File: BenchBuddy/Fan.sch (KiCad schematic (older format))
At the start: 0 parts

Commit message: Week3 part 1
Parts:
- added Q?: MOSFET_N, ~, symbol MOSFET_N
- added R? (x5): R, ~, symbol R
- added RV?: POT, ~, symbol POT
- added U?: LM324, symbol LM324
- added U?: MCP4922-E/P, DIP14, symbol MCP4922-E/P
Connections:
- net labels added: +12V, -12V, AGND, CS_N, Current Measure, MISO, MOSI, SLCK
- wire segments 0 -> 34

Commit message: Week3 Part 2
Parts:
- removed R? (x3): R, ~, symbol R
- removed RV?: POT, ~, symbol POT
- added D?: DIODE, ~, symbol DIODE
- added Q? (x2): MOSFET_N, ~, symbol MOSFET_N
- added TH?: THERMISTOR, ~, symbol THERMISTOR
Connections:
- net labels added: +12C, CURR_MEAS, FAN_MODE, FAN_PWM, Fan_Out+, Fan_Out-, Tach_In, Tach_MEASURE
- net labels removed: Current Measure, Fan_IN, Power+, Power-, Tach, Tach_OUT
- wire segments 34 -> 36
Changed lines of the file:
@@
 EESchema Schematic File Version 2
+LIBS:BenchBuddy
 LIBS:power
 LIBS:device
@@
 $Descr A4 11693 8268
 encoding utf-8
-Sheet 7 9
+Sheet 9 9
 Title ""
-Date "5 mar 2014"
+Date "7 mar 2014"
 Rev ""
 Comp ""
@@
 Comment4 ""
 $EndDescr
-Text HLabel 9800 3350 0    60   Output ~ 0
-Power+
-Text HLabel 9800 3650 0    60   Input ~ 0
-Power-
-Text HLabel 9750 3900 0    60   Input ~ 0
-Tach
-Text HLabel 1300 4300 0    60   Output ~ 0
-Tach_OUT
+Text HLabel 9800 2000 2    60   Output ~ 0
+Fan_Out+
+Text HLabel 9800 2150 2    60   Output ~ 0
+Fan_Out-
+Text HLabel 9800 6150 2    60   Input ~ 0
+Tach_In
+Text HLabel 1250 6150 0    60   Output ~ 0
+Tach_MEASURE
 Text HLabel 1300 4050 0    60   Input ~ 0
-Fan_IN
+FAN_PWM
 $Comp
 L LM324 U?
@@
 F 3 "~" H 7550 2550 60  0000 C CNN
 	1    7550 2550
-	1    0    0    -1
-$EndComp
-$Comp
-L +12V #PWR?
-U 1 1 531512F4
-P 7650 1950
-F 0 "#PWR?" H 7650 1900 20  0001 C CNN
-F 1 "+12V" H 7650 2050 30  0000 C CNN
-F 2 "" H 7650 1950 60  0000 C CNN
-F 3 "" H 7650 1950 60  0000 C CNN
-	1    7650 1950
 	1    0    0    -1
 $EndComp
@@
 $EndComp
 $Comp
-L R R?
-U 1 1 53151457
-P 4650 2150
-F 0 "R?" V 4730 2150 40  0000 C CNN
-F 1 "R" V 4657 2151 40  0000 C CNN
-F 2 "~" V 4580 2150 30  0000 C CNN
-F 3 "~" H 4650 2150 30  0000 C CNN
-	1    4650 2150
-	1    0    0    -1
-$EndComp
-$Comp
 L +12V #PWR?
 U 1 1 53151465
@@
 	6700 2550 7350 2550
 Wire Wire Line
-	7650 1950 7650 2350
-Wire Wire Line
-	7650 2750 7650 3350
-Wire Wire Line
-	7650 3350 9800 3350
-Wire Wire Line
-	5550 3650 9800 3650
-Wire Wire Line
-	7650 3650 7650 4100
-Wire Wire Line
 	7650 4600 7650 4900
 Wire Wire Line
-	5550 3650 5550 2650
-Wire Wire Line
 	5550 2650 5700 2650
-Connection ~ 7650 3650
 Wire Wire Line
 	6100 3150 6100 2950
@@
 Wire Wire Line
 	4400 2450 5700 2450
-Wire Wire Line
-	4650 2400 4650 3000
-Connection ~ 4650 2450
-$Comp
-L POT RV?
-U 1 1 531514B9
-P 4650 3250
-F 0 "RV?" H 4650 3150 50  0000 C CNN
-F 1 "POT" H 4650 3250 50  0000 C CNN
-F 2 "~" H 4650 3250 60  0000 C CNN
-F 3 "~" H 4650 3250 60  0000 C CNN
-	1    4650 3250
-	0    -1   -1   0
-$EndComp
-Wire Wire Line
-	4650 3500 4650 3850
 $Comp
 L AGND #PWR?
 U 1 1 53151500
-P 4650 3850
-F 0 "#PWR?" H 4650 3850 40  0001 C CNN
-F 1 "AGND" H 4650 3780 50  0000 C CNN
-F 2 "" H 4650 3850 60  0000 C CNN
-F 3 "" H 4650 3850 60  0000 C CNN
-	1    4650 3850
-	1    0    0    -1
-$EndComp
-Wire Wire Line
-	8200 3900 9750 3900
+P 5200 3250
+F 0 "#PWR?" H 5200 3250 40  0001 C CNN
+F 1 "AGND" H 5200 3180 50  0000 C CNN
+F 2 "" H 5200 3250 60  0000 C CNN
+F 3 "" H 5200 3250 60  0000 C CNN
+	1    5200 3250
+	1    0    0    -1
+$EndComp
 Text HLabel 1300 4150 0    60   Input ~ 0
-Current Measure
-Wire Wire Line
-	1300 4150 5650 4150
-Connection ~ 7650 4000
-$Comp
-L R R?
-U 1 1 5315166D
-P 5200 3250
-F 0 "R?" V 5280 3250 40  0000 C CNN
-F 1 "R" V 5207 3251 40  0000 C CNN
-F 2 "~" V 5130 3250 30  0000 C CNN
-F 3 "~" H 5200 3250 30  0000 C CNN
-	1    5200 3250
-	1    0    0    -1
-$EndComp
-Wire Wire Line
-	1300 4050 4950 4050
-Wire Wire Line
-	4950 4050 4950 3650
-Wire Wire Line
-	4950 3650 5200 3650
-Wire Wire Line
-	5200 3650 5200 3550
-Wire Wire Line
-	5200 3000 5200 2450
-Connection ~ 5200 2450
-Wire Wire Line
-	5650 4150 5650 4000
-Wire Wire Line
-	1300 4300 5650 4300
-Wire Wire Line
-	5650 4300 5650 5200
-Wire Wire Line
-	5650 5200 8200 5200
-Wire Wire Line
-	8200 5200 8200 3900
-Wire Wire Line
-	5650 4000 7650 4000
+CURR_MEAS
+Wire Wire Line
+	5650 4150 1300 4150
+Wire Wire Line
+	5650 3800 5650 4150
+Wire Wire Line
+	1250 6150 9800 6150
 $Comp
 L MCP4922-E/P U?
@@
 Wire Wire Line
 	2450 2600 1300 2600
-$Comp
-L R R?
-U 1 1 5315191D
-P 2450 3350
-F 0 "R?" V 2530 3350 40  0000 C CNN
-F 1 "R" V 2457 3351 40  0000 C CNN
-F 2 "~" V 2380 3350 30  0000 C CNN
-F 3 "~" H 2450 3350 30  0000 C CNN
-	1    2450 3350
-	1    0    0    -1
-$EndComp
-Wire Wire Line
-	2450 3100 2450 2800
-Wire Wire Line
-	2450 3600 2450 4050
+Wire Wire Line
+	2450 2800 2450 4050
 Connection ~ 2450 4050
+$Comp
+L MOSFET_N Q?
+U 1 1 53191BE7
+P 7050 4350
+F 0 "Q?" H 7060 4520 60  0000 R CNN
+F 1 "MOSFET_N" H 7060 4200 60  0000 R CNN
+F 2 "~" H 7050 4350 60  0000 C CNN
+F 3 "~" H 7050 4350 60  0000 C CNN
+	1    7050 4350
+	1    0    0    -1
+$EndComp
+$Comp
+L THERMISTOR TH?
+U 1 1 53191C1C
+P 7650 1350
+F 0 "TH?" V 7750 1400 50  0000 C CNN
+F 1 "THERMISTOR" V 7550 1350 50  0000 C CNN
+F 2 "~" H 7650 1350 60  0000 C CNN
+F 3 "~" H 7650 1350 60  0000 C CNN
+	1    7650 1350
+	1    0    0    -1
+$EndComp
+Wire Wire Line
+	7650 1100 7650 1000
+Wire Wire Line
+	7650 1600 7650 2000
+Wire Wire Line
+	7650 2000 9800 2000
+Wire Wire Line
+	9800 2150 7650 2150
+Wire Wire Line
+	7650 2150 7650 2350
+$Comp
+L DIODE D?
+U 1 1 53191C9A
+P 7450 2000
+F 0 "D?" H 7450 2100 40  0000 C CNN
+F 1 "DIODE" H 7450 1900 40  0000 C CNN
+F 2 "~" H 7450 2000 60  0000 C CNN
+F 3 "~" H 7450 2000 60  0000 C CNN
+	1    7450 2000
+	0    -1   -1   0
+$EndComp
+Wire Wire Line
+	7450 2200 7650 2200
+Connection ~ 7650 2200
+Wire Wire Line
+	7450 1800 7650 1800
+Connection ~ 7650 1800
+Wire Wire Line
+	7650 2750 7650 4100
+Wire Wire Line
+	7150 4150 7150 3950
+Wire Wire Line
+	7150 3950 7650 3950
+Connection ~ 7650 3950
+Wire Wire Line
+	7150 4550 7150 4750
+Wire Wire Line
+	7150 4750 7650 4750
+Connection ~ 7650 4750
+Wire Wire Line
+	5650 3800 7650 3800
+Connection ~ 7650 3800
+Wire Wire Line
+	1300 4050 3800 4050
+Wire Wire Line
+	5550 3500 7650 3500
+Connection ~ 7650 3500
+Wire Wire Line
+	5550 3500 5550 2650
+$Comp
+L MOSFET_N Q?
+U 1 1 53191E78
+P 5100 2900
+F 0 "Q?" H 5110 3070 60  0000 R CNN
+F 1 "MOSFET_N" H 5110 2750 60  0000 R CNN
+F 2 "~" H 5100 2900 60  0000 C CNN
+F 3 "~" H 5100 2900 60  0000 C CNN
+	1    5100 2900
+	1    0    0    -1
+$EndComp
+Wire Wire Line
+	5200 3250 5200 3100
+Wire Wire Line
+	5200 2700 5200 2450
+Connection ~ 5200 2450
+Wire Wire Line
+	4900 2900 3800 2900
+Wire Wire Line
+	3800 2900 3800 4050
+Text HLabel 1300 4350 0    60   Input ~ 0
+FAN_MODE
+Wire Wire Line
+	1300 4350 6850 4350
+$Comp
+L +12C #PWR?
+U 1 1 53192305
+P 7650 1000
+F 0 "#PWR?" H 7650 970 30  0001 C CNN
+F 1 "+12C" H 7650 1110 40  0000 C CNN
+F 2 "~" H 7650 1000 60  0000 C CNN
+F 3 "~" H 7650 1000 60  0000 C CNN
+	1    7650 1000
+	1    0    0    -1
+$EndComp
 $EndSCHEMATC

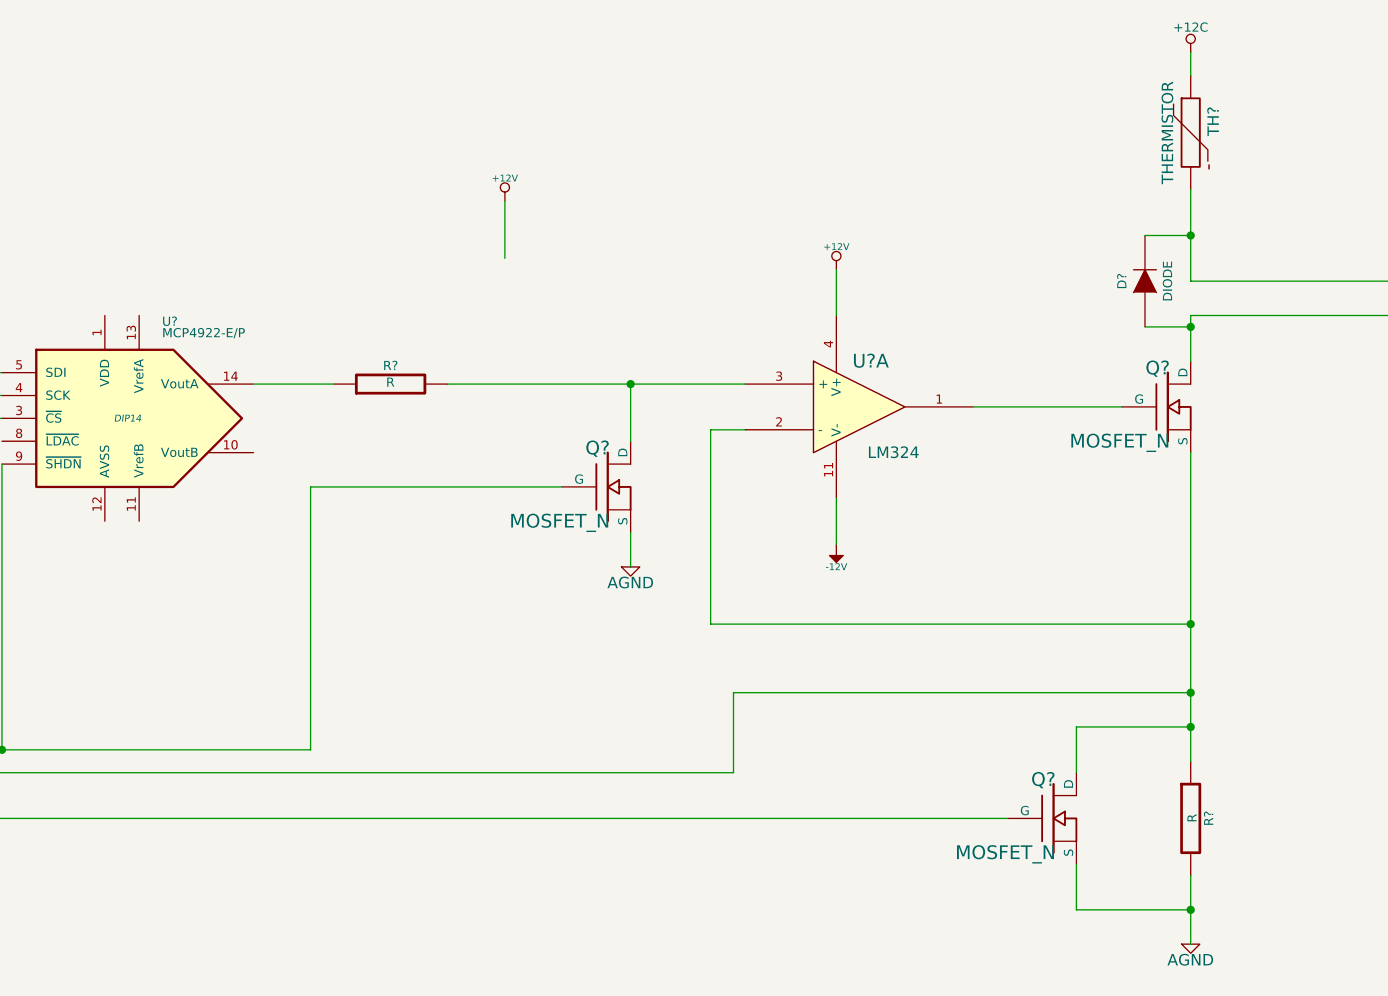
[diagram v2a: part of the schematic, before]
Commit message: Colocação dos Componentes Relé
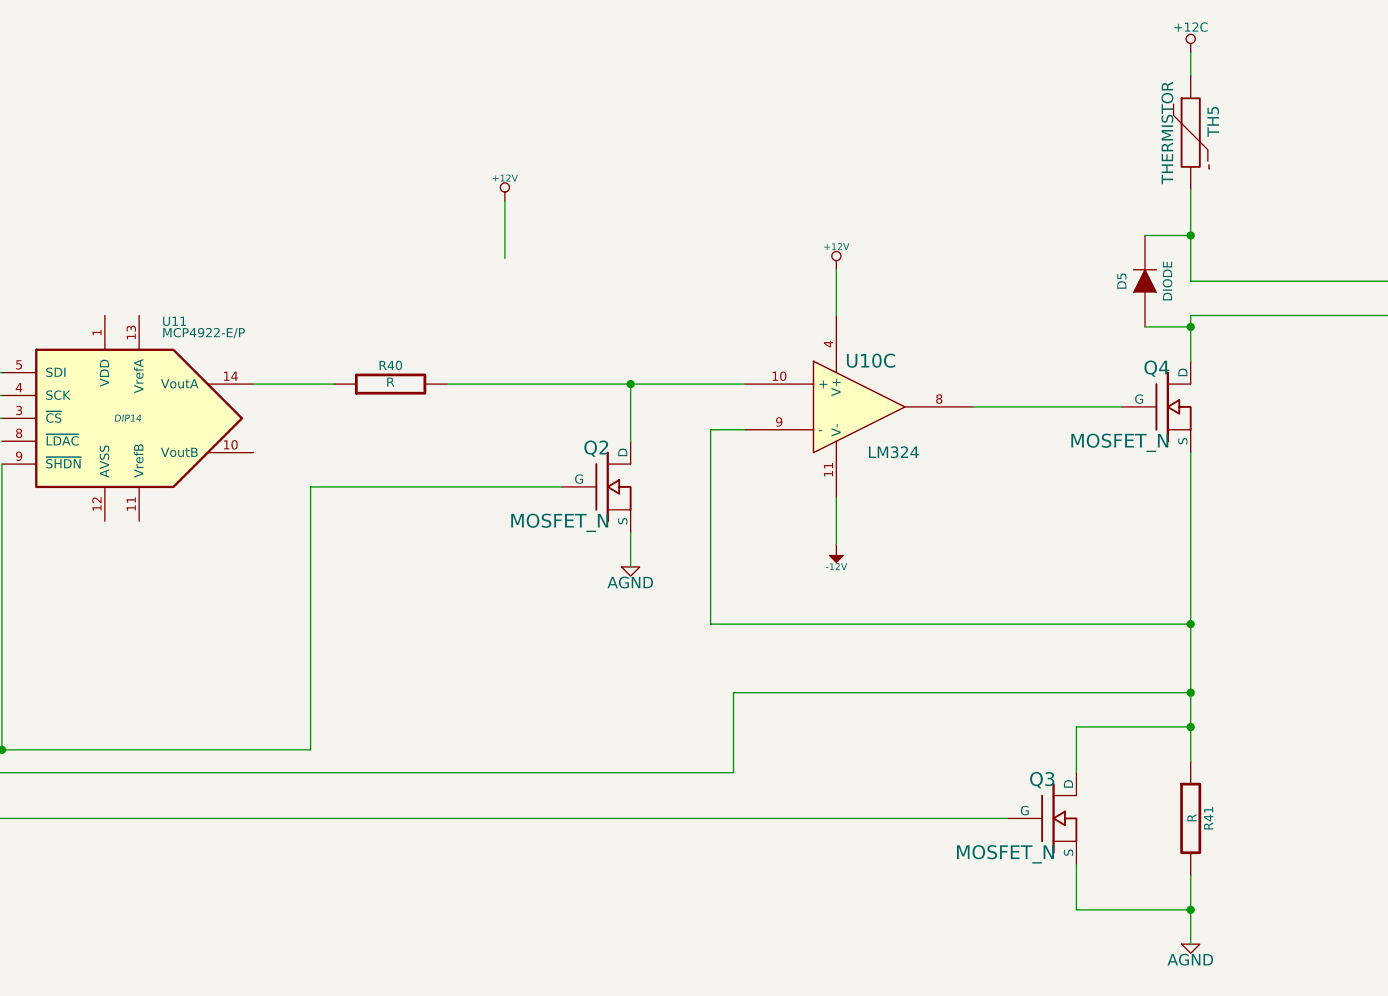
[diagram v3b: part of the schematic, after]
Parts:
- gave numbers to parts that had none: 9
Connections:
- net CURR_MEAS: now also U10.9 (-); no longer U10.2 (-)
- net at Q4.G: now also U10.8; no longer U10.1
- net at Q2.D, R40.2: now also U10.10 (+); no longer U10.3 (+)
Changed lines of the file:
@@
 Sheet 9 9
 Title ""
-Date "7 mar 2014"
+Date "9 mar 2014"
 Rev ""
 Comp ""
@@
 FAN_PWM
 $Comp
-L LM324 U?
-U 1 1 5315125A
+L LM324 U10
+U 3 1 5315125A
 P 6200 2550
-F 0 "U?" H 6250 2750 60  0000 C CNN
+F 0 "U10" H 6250 2750 60  0000 C CNN
 F 1 "LM324" H 6350 2350 50  0000 C CNN
 F 2 "" H 6200 2550 60  0000 C CNN
 F 3 "" H 6200 2550 60  0000 C CNN
-	1    6200 2550
-	1    0    0    -1
-$EndComp
-$Comp
-L MOSFET_N Q?
+	3    6200 2550
+	1    0    0    -1
+$EndComp
+$Comp
+L MOSFET_N Q4
 U 1 1 531512AB
 P 7550 2550
-F 0 "Q?" H 7560 2720 60  0000 R CNN
+F 0 "Q4" H 7560 2720 60  0000 R CNN
 F 1 "MOSFET_N" H 7560 2400 60  0000 R CNN
 F 2 "~" H 7550 2550 60  0000 C CNN
@@
 $EndComp
 $Comp
-L R R?
+L R R41
 U 1 1 53151349
 P 7650 4350
-F 0 "R?" V 7730 4350 40  0000 C CNN
+F 0 "R41" V 7730 4350 40  0000 C CNN
 F 1 "R" V 7657 4351 40  0000 C CNN
 F 2 "~" V 7580 4350 30  0000 C CNN
@@
 $EndComp
 $Comp
-L AGND #PWR?
+L AGND #PWR55
 U 1 1 53151369
 P 7650 4900
-F 0 "#PWR?" H 7650 4900 40  0001 C CNN
+F 0 "#PWR55" H 7650 4900 40  0001 C CNN
 F 1 "AGND" H 7650 4830 50  0000 C CNN
 F 2 "" H 7650 4900 60  0000 C CNN
@@
 $EndComp
 $Comp
-L +12V #PWR?
+L +12V #PWR52
 U 1 1 531513AA
 P 6100 1950
-F 0 "#PWR?" H 6100 1900 20  0001 C CNN
+F 0 "#PWR52" H 6100 1900 20  0001 C CNN
 F 1 "+12V" H 6100 2050 30  0000 C CNN
 F 2 "" H 6100 1950 60  0000 C CNN
@@
 $EndComp
 $Comp
-L -12V #PWR?
+L -12V #PWR53
 U 1 1 531513F2
 P 6100 3150
-F 0 "#PWR?" H 6100 3280 20  0001 C CNN
+F 0 "#PWR53" H 6100 3280 20  0001 C CNN
 F 1 "-12V" H 6100 3250 30  0000 C CNN
 F 2 "" H 6100 3150 60  0000 C CNN
@@
 $EndComp
 $Comp
-L +12V #PWR?
+L +12V #PWR50
 U 1 1 53151465
 P 4650 1650
-F 0 "#PWR?" H 4650 1600 20  0001 C CNN
+F 0 "#PWR50" H 4650 1600 20  0001 C CNN
 F 1 "+12V" H 4650 1750 30  0000 C CNN
 F 2 "" H 4650 1650 60  0000 C CNN
@@
 	4400 2450 5700 2450
 $Comp
-L AGND #PWR?
+L AGND #PWR51
 U 1 1 53151500
 P 5200 3250
-F 0 "#PWR?" H 5200 3250 40  0001 C CNN
+F 0 "#PWR51" H 5200 3250 40  0001 C CNN
 F 1 "AGND" H 5200 3180 50  0000 C CNN
 F 2 "" H 5200 3250 60  0000 C CNN
@@
 	1250 6150 9800 6150
 $Comp
-L MCP4922-E/P U?
+L MCP4922-E/P U11
 U 1 1 531517BB
 P 3000 2600
-F 0 "U?" H 3150 3000 40  0000 L BNN
+F 0 "U11" H 3150 3000 40  0000 L BNN
 F 1 "MCP4922-E/P" H 3150 2950 40  0000 L BNN
 F 2 "DIP14" H 3000 2600 30  0000 C CIN
@@
 $EndComp
 $Comp
-L R R?
+L R R40
 U 1 1 531517D2
 P 4150 2450
-F 0 "R?" V 4230 2450 40  0000 C CNN
+F 0 "R40" V 4230 2450 40  0000 C CNN
 F 1 "R" V 4157 2451 40  0000 C CNN
 F 2 "~" V 4080 2450 30  0000 C CNN
@@
 Connection ~ 2450 4050
 $Comp
-L MOSFET_N Q?
+L MOSFET_N Q3
 U 1 1 53191BE7
 P 7050 4350
-F 0 "Q?" H 7060 4520 60  0000 R CNN
+F 0 "Q3" H 7060 4520 60  0000 R CNN
 F 1 "MOSFET_N" H 7060 4200 60  0000 R CNN
 F 2 "~" H 7050 4350 60  0000 C CNN
@@
 $EndComp
 $Comp
-L THERMISTOR TH?
+L THERMISTOR TH5
 U 1 1 53191C1C
 P 7650 1350
-F 0 "TH?" V 7750 1400 50  0000 C CNN
+F 0 "TH5" V 7750 1400 50  0000 C CNN
 F 1 "THERMISTOR" V 7550 1350 50  0000 C CNN
 F 2 "~" H 7650 1350 60  0000 C CNN
@@
 	7650 2150 7650 2350
 $Comp
-L DIODE D?
+L DIODE D5
 U 1 1 53191C9A
 P 7450 2000
-F 0 "D?" H 7450 2100 40  0000 C CNN
+F 0 "D5" H 7450 2100 40  0000 C CNN
 F 1 "DIODE" H 7450 1900 40  0000 C CNN
 F 2 "~" H 7450 2000 60  0000 C CNN
@@
 	5550 3500 5550 2650
 $Comp
-L MOSFET_N Q?
+L MOSFET_N Q2
 U 1 1 53191E78
 P 5100 2900
-F 0 "Q?" H 5110 3070 60  0000 R CNN
+F 0 "Q2" H 5110 3070 60  0000 R CNN
 F 1 "MOSFET_N" H 5110 2750 60  0000 R CNN
 F 2 "~" H 5100 2900 60  0000 C CNN
@@
 	1300 4350 6850 4350
 $Comp
-L +12C #PWR?
+L +12C #PWR54
 U 1 1 53192305
 P 7650 1000
-F 0 "#PWR?" H 7650 970 30  0001 C CNN
+F 0 "#PWR54" H 7650 970 30  0001 C CNN
 F 1 "+12C" H 7650 1110 40  0000 C CNN
 F 2 "~" H 7650 1000 60  0000 C CNN

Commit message: Pre layout
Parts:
- removed Q2, Q3, Q4: MOSFET_N, ~, symbol MOSFET_N
- removed U11: MCP4922-E/P, DIP14, symbol MCP4922-E/P
- added C11, C12: C, ~, symbol C
- added Q2: DMN65D8L-7, ~, symbol MOS_N
- added Q3, Q4: AOD476, ~, symbol MOS_N_NUNBERS
- added U11: MCP4801, symbol MCP4801
- D5: value DIODE -> B130-13-F; MFG Name (none) -> DIODES INCORPORATED; MFG Part Number (none) -> B130-13-F
- TH5: value THERMISTOR -> MINISMDC050F-2; MFG Name (none) -> TE CONNECTIVITY; MFG Part Number (none) -> MINISMDC050F-2
- U4: renamed from U10; value LM324 -> OPA4170
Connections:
- net labels added: +5V, FE_V+, FE_V-, GND_FAN, ~LDAC, ~SHDN
- net labels removed: +12V, -12V, MISO
- wire segments 36 -> 44
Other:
- moved on the sheet: D5, R40, R41, TH5
